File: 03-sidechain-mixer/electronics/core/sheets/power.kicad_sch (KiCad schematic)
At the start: 9 parts, among them J3 Conn_02x05_Odd_Even, J4 Conn_01x02, J5 Conn_02x03_Odd_Even

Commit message: Prepared sidechain mixer PCB
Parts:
- C23, C24, D6, D7, J3, J4, J5, TP12, TP13: CHECKED YES -> (none)
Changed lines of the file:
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@@
 			)
 		)
-		(property "CHECKED" "YES"
+		(property "CHECKED" ""
+			(at 231.14 91.44 0)
+			(effects
+				(font
+					(size 1.27 1.27)
+				)
+				(hide yes)
+			)
+		)
+		(property "Arwill" ""
+			(at 231.14 91.44 0)
+			(effects
+				(font
+					(size 1.27 1.27)
+				)
+				(hide yes)
+			)
+		)
+		(property "Hestore" ""
 			(at 231.14 91.44 0)
 			(effects
@@
 			)
 		)
-		(property "CHECKED" "YES"
+		(property "CHECKED" ""
+			(at 175.26 106.68 0)
+			(effects
+				(font
+					(size 1.27 1.27)
+				)
+				(hide yes)
+			)
+		)
+		(property "Arwill" ""
+			(at 175.26 106.68 0)
+			(effects
+				(font
+					(size 1.27 1.27)
+				)
+				(hide yes)
+			)
+		)
+		(property "Hestore" ""
 			(at 175.26 106.68 0)
 			(effects
@@
 			)
 		)
-		(property "CHECKED" "YES"
+		(property "CHECKED" ""
 			(at 88.9 92.71 0)
 			(effects
@@
 		)
 		(property "Mouser Part no." "200-TSW10307TD"
+			(at 88.9 92.71 0)
+			(effects
+				(font
+					(size 1.27 1.27)
+				)
+				(hide yes)
+			)
+		)
+		(property "Arwill" ""
+			(at 88.9 92.71 0)
+			(effects
+				(font
+					(size 1.27 1.27)
+				)
+				(hide yes)
+			)
+		)
+		(property "Hestore" ""
 			(at 88.9 92.71 0)
 			(effects
@@
 			)
 		)
-		(property "CHECKED" "YES"
+		(property "CHECKED" ""
+			(at 231.14 99.06 0)
+			(effects
+				(font
+					(size 1.27 1.27)
+				)
+				(hide yes)
+			)
+		)
+		(property "Arwill" ""
+			(at 231.14 99.06 0)
+			(effects
+				(font
+					(size 1.27 1.27)
+				)
+				(hide yes)
+			)
+		)
+		(property "Hestore" ""
 			(at 231.14 99.06 0)
 			(effects
@@
 			)
 		)
-		(property "CHECKED" "YES"
+		(property "CHECKED" ""
 			(at 156.21 97.79 0)
 			(effects
@@
 		)
 		(property "Mouser Part no." "571-5103310-1"
+			(at 156.21 97.79 0)
+			(effects
+				(font
+					(size 1.27 1.27)
+				)
+				(hide yes)
+			)
+		)
+		(property "Arwill" ""
+			(at 156.21 97.79 0)
+			(effects
+				(font
+					(size 1.27 1.27)
+				)
+				(hide yes)
+			)
+		)
+		(property "Hestore" ""
 			(at 156.21 97.79 0)
 			(effects
@@
 			)
 		)
-		(property "CHECKED" "YES"
+		(property "CHECKED" ""
+			(at 173.99 85.09 0)
+			(effects
+				(font
+					(size 1.27 1.27)
+				)
+				(hide yes)
+			)
+		)
+		(property "Arwill" ""
+			(at 173.99 85.09 0)
+			(effects
+				(font
+					(size 1.27 1.27)
+				)
+				(hide yes)
+			)
+		)
+		(property "Hestore" ""
 			(at 173.99 85.09 0)
 			(effects
@@
 			)
 		)
-		(property "CHECKED" "YES"
+		(property "CHECKED" ""
+			(at 187.96 107.95 0)
+			(effects
+				(font
+					(size 1.27 1.27)
+				)
+				(hide yes)
+			)
+		)
+		(property "Arwill" ""
+			(at 187.96 107.95 0)
+			(effects
+				(font
+					(size 1.27 1.27)
+				)
+				(hide yes)
+			)
+		)
+		(property "Hestore" ""
 			(at 187.96 107.95 0)
 			(effects
@@
 			)
 		)
-		(property "CHECKED" "YES"
+		(property "CHECKED" ""
 			(at 92.71 109.22 0)
 			(effects
@@
 		)
 		(property "Mouser Part no." "200-HTSW10207TS"
+			(at 92.71 109.22 0)
+			(effects
+				(font
+					(size 1.27 1.27)
+				)
+				(hide yes)
+			)
+		)
+		(property "Arwill" ""
+			(at 92.71 109.22 0)
+			(effects
+				(font
+					(size 1.27 1.27)
+				)
+				(hide yes)
+			)
+		)
+		(property "Hestore" ""
 			(at 92.71 109.22 0)
 			(effects
@@
 			)
 		)
-		(property "CHECKED" "YES"
+		(property "CHECKED" ""
 			(at 187.96 83.82 0)
 			(effects
+				(font
+					(size 1.27 1.27)
+				)
+				(hide yes)
+			)
+		)
+		(property "Arwill" ""
+			(at 187.96 83.82 0)
+			(effects
+				(font
+					(size 1.27 1.27)
+				)
+				(hide yes)
+			)
+		)
+		(property "Hestore" ""
+			(at 187.96 83.82 0)
+			(effects

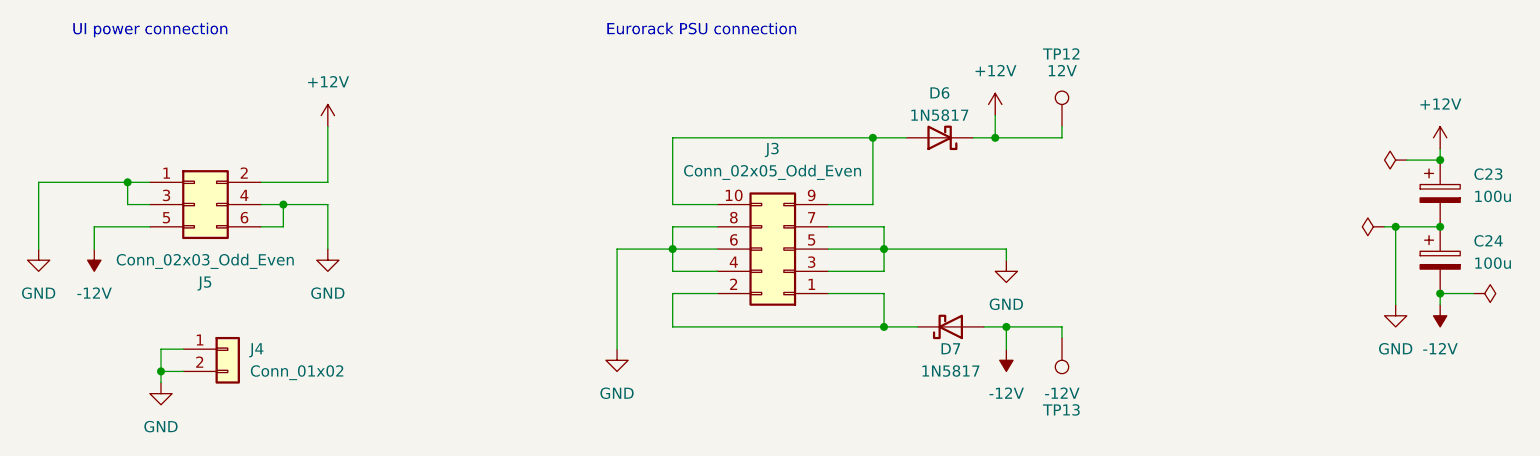
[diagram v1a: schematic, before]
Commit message: SC-Mixer PCB base done
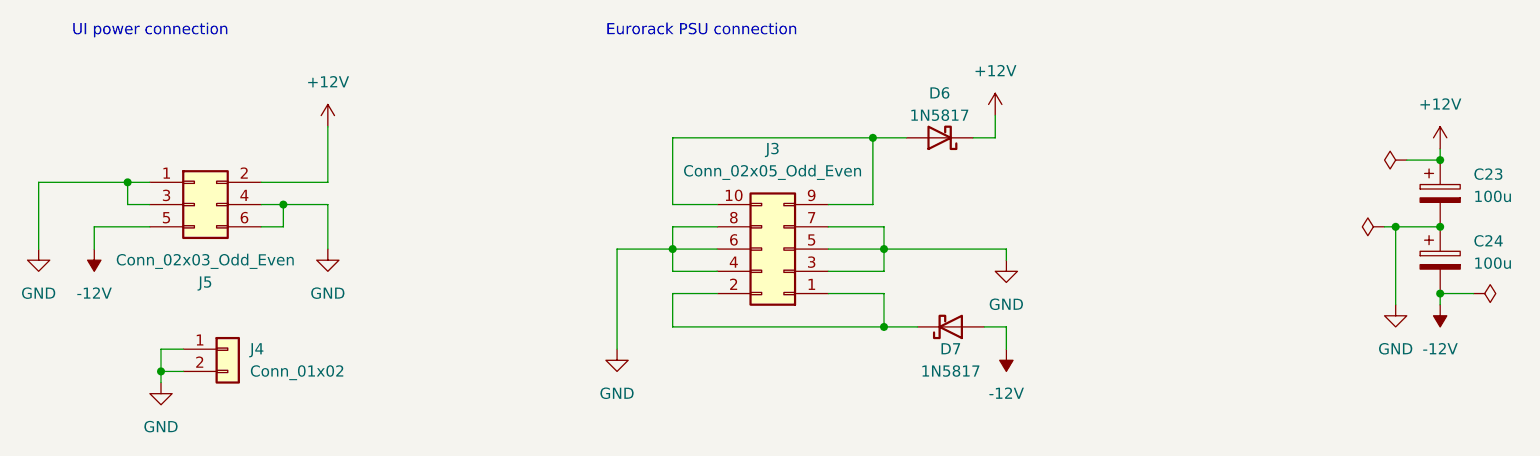
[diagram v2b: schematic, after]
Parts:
- removed TP12: 12V, TestPoint:TestPoint_THTPad_2.0x2.0mm_Drill1.0mm, symbol Connector:TestPoint
- removed TP13: -12V, TestPoint:TestPoint_THTPad_2.0x2.0mm_Drill1.0mm, symbol Connector:TestPoint

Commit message: Checked all components on SC-Mixer
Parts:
- C23, C24, D6, D7: CHECKED (none) -> YES
- J3: Mouser Part no. 571-5103310-1 -> (none); Part URL https://mou.sr/3GwYxj9 -> (none)
- J4: Mouser Part no. 200-HTSW10207TS -> (none); Part URL https://mou.sr/3IruU3e -> (none)
- J5: Mouser Part no. 200-TSW10307TD -> (none); Part URL https://mou.sr/4liCQlU -> (none)
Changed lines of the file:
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@@
 			)
 		)
-		(property "CHECKED" ""
+		(property "CHECKED" "YES"
 			(at 231.14 91.44 0)
 			(effects
@@
 			)
 		)
-		(property "CHECKED" ""
+		(property "CHECKED" "YES"
 			(at 175.26 106.68 0)
 			(effects
@@
 			)
 		)
-		(property "Part URL" "https://mou.sr/4liCQlU"
+		(property "Part URL" ""
 			(at 88.9 92.71 0)
 			(effects
@@
 			)
 		)
-		(property "Mouser Part no." "200-TSW10307TD"
+		(property "Mouser Part no." ""
 			(at 88.9 92.71 0)
 			(effects
@@
 			)
 		)
-		(property "CHECKED" ""
+		(property "CHECKED" "YES"
 			(at 231.14 99.06 0)
 			(effects
@@
 			)
 		)
-		(property "Part URL" "https://mou.sr/3GwYxj9"
+		(property "Part URL" ""
 			(at 156.21 97.79 0)
 			(effects
@@
 			)
 		)
-		(property "Mouser Part no." "571-5103310-1"
+		(property "Mouser Part no." ""
 			(at 156.21 97.79 0)
 			(effects
@@
 			)
 		)
-		(property "CHECKED" ""
+		(property "CHECKED" "YES"
 			(at 173.99 85.09 0)
 			(effects
@@
 			)
 		)
-		(property "Part URL" "https://mou.sr/3IruU3e"
+		(property "Part URL" ""
 			(at 92.71 109.22 0)
 			(effects
@@
 			)
 		)
-		(property "Mouser Part no." "200-HTSW10207TS"
+		(property "Mouser Part no." ""
 			(at 92.71 109.22 0)
 			(effects
